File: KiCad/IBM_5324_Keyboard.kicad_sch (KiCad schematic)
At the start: 104 parts, among them J1 To 5324, J2 To DB25, SW1 CMD, SW10 ERASE, SW11 | 1, SW12 # 3, SW13 % 5, SW14 & 7, SW15 ( 9, SW16 _ -, SW17 RH <-, SW18 NP 8, SW19 / -, SW2 ~ `, SW20 HOLD, SW21 FIELD ADV, SW22 W, SW23 R, SW24 Y, SW25 I, SW26 P, SW27 | \, SW28 NP 7, SW29 NP 9, SW3 @ 2, SW30 INQ, SW31 SHIFT LOCK, SW32 Q, SW33 E, SW34 T, SW35 U, SW36 O, SW37 ! ¢, SW38 ENTER, SW39 NP 4, SW4 $ 4, SW40 FIELD-, SW41 ERROR RESET, SW42 LH SHIFT, SW43 A, SW44 D, SW45 G, SW46 J, SW47 L, SW48 " ', SW49 } {, SW5 ^ 6, SW50 NP 5, SW51 NP 6, SW52 TEST, SW53 SCROLL DOWN, SW54 S, SW55 F, SW56 H, SW57 K, SW58 : ;, SW59 NEWLINE, SW6 * 8, SW60 NP 1, SW61 NP 3, SW62 SCROLL UP, SW63 ->, SW64 > <, SW65 C, SW66 B, SW67 N, SW68 M, SW69 . ., SW7 ) 0, SW70 RH SHIFT, SW71 NP 2, SW72 FIELD+, SW73 LH <-, SW74 ALT, SW75 Z, SW76 X, SW77 V, SW78 SPACE, SW79 , ,, SW8 + =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

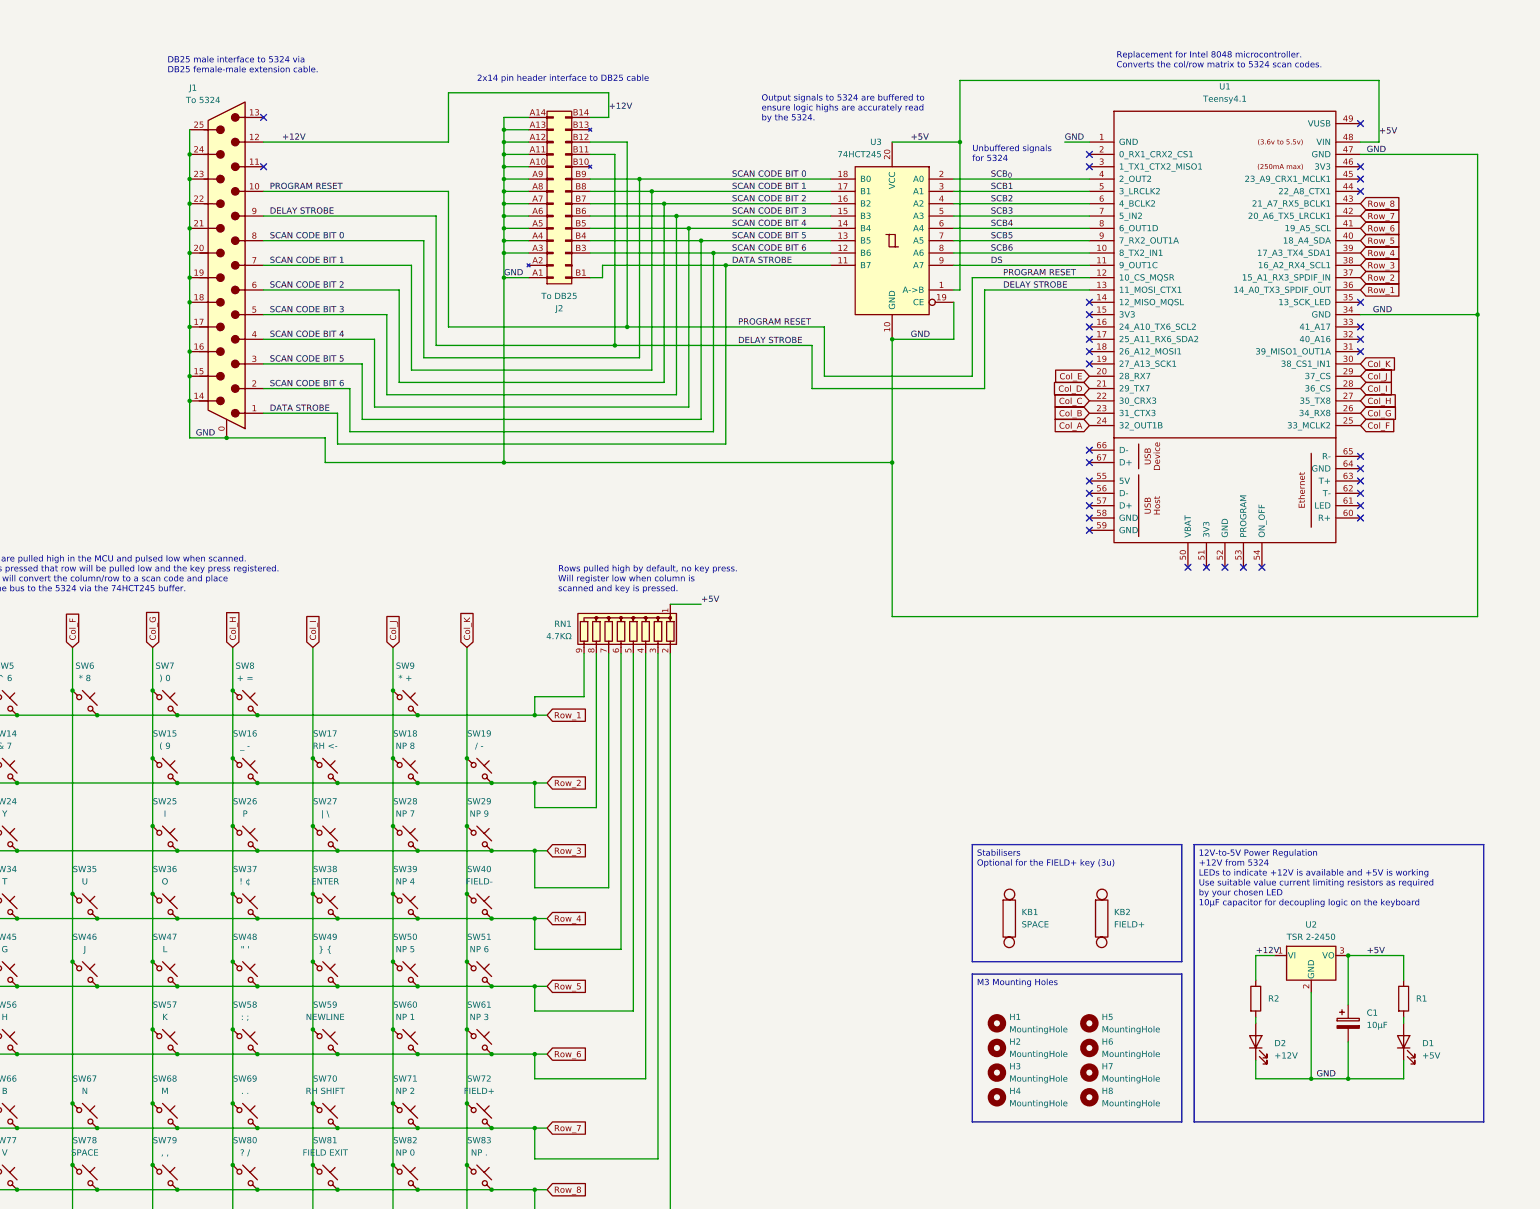
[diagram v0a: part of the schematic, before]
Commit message: Added 74LS125 buffer for incoming signals
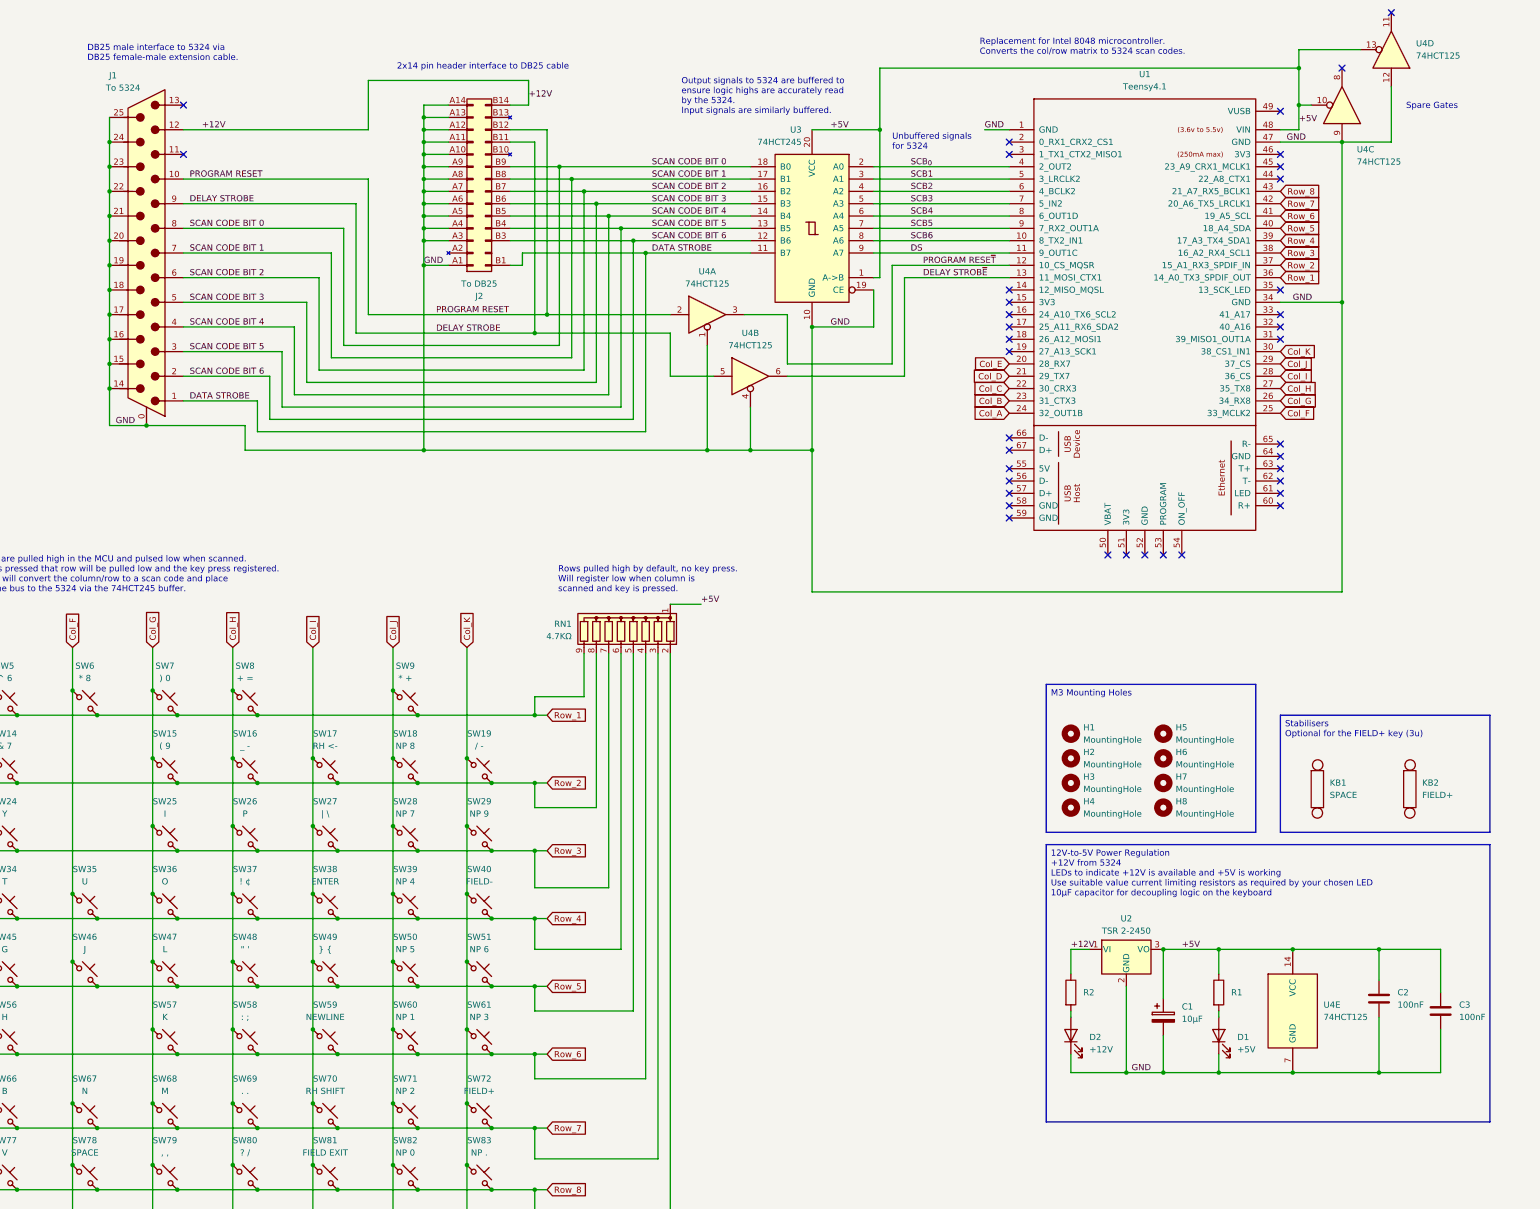
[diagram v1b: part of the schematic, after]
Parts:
- added C2, C3: 100nF, Capacitor_THT:C_Disc_D3.8mm_W2.6mm_P2.50mm, symbol Device:C
- added U4: 74HCT125, Package_DIP:DIP-14_W7.62mm, symbol 74xx:74LS125
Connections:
- net +5V: now also C2.1, C3.1, U4.10, U4.13, U4.14 (VCC)
- net DELAY STROBE: now also U4.5; no longer U1.13 (11_MOSI_CTX1)
- net GND: now also C2.2, C3.2, U4.1, U4.12, U4.4, U4.7 (GND), U4.9
- net PROGRAM RESET: now also U4.2; no longer U1.12 (10_CS_MQSR)
- new net DELAY STROB~{E}: U1.13 (11_MOSI_CTX1), U4.6
- new net PROGRAM RESE~{T}: U1.12 (10_CS_MQSR), U4.3
- no-connect marks 36 -> 38
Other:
- note added: "Output signals to 5324 are buffered to ensure logic highs are accurately read by the 5324. Input signals are similarly buffered."
- note added: "Spare Gates"
- note removed: "Output signals to 5324 are buffered to ensure logic highs are accurately read by the 5324."
- moved on the sheet: C1, D1, D2, H1, H2, H3, H4, H5, H6, H7, H8, J1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
